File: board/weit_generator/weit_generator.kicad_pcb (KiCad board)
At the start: 2 copper layers, 58 parts, among them J1 POWER, J2 PROG, J3 OUTPUT, Q1 BC547, U1 MCP6004, U2 AVR32DA28x-xSO, U3 LM4041L, U4 LMV321, X1 SG-5032CAN

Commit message: .
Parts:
- moved C1 83.8 mm to (131.2, 80.8), turned to 180 degrees
- moved J2 76.5 mm to (123.2, 91.8), turned to 180 degrees
- moved J1 41.5 mm to (131.3, 86.8), turned to -90 degrees
- moved C7 40.4 mm to (138.1, 86.1)
- moved C6 39.7 mm to (138.1, 79.5)
- moved J3 39.5 mm to (148.4, 93.1)
- moved C4 38.9 mm to (127.3, 92.9), turned to 0 degrees
- moved U4 25.2 mm to (142.8, 93.2), turned to 180 degrees
- moved Q1 19.4 mm to (116.4, 130.4), turned to 0 degrees
- moved R2 18.0 mm to (126.6, 104.7), turned to -90 degrees
- moved R29 17.7 mm to (112.9, 125.0)
- moved RV1 17.1 mm to (123.4, 117.6), turned to 90 degrees
- moved TP3 14.7 mm to (149.1, 127.0)
- moved C2 14.1 mm to (117.8, 122.7), turned to 90 degrees
- moved R27 13.3 mm to (122.1, 125.7), turned to 0 degrees
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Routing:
- net +3V0: track 33.2 -> 134.4 mm
- net GND: track 11.6 -> 27.8 mm
- net Net-(U1C--): track 38.2 -> 24.2 mm
- net /Autogain/OUT: track 4.72 -> 17.5 mm
- net Net-(U1A--): track 9.35 -> 19.3 mm
- net /R-2R DAC/OUT: track 3.57 -> 12.3 mm
- net Net-(J2-Pin_2): track 5.18 -> 12.8 mm
- net Net-(U1C-+): track 13.5 -> 20.8 mm
- net Net-(C13-Pad1): track 26.1 -> 19.3 mm
- net Net-(C11-Pad2): track 21.5 -> 15.5 mm
- net Net-(U1D-+): track 12.7 -> 16.9 mm
- net Net-(J2-Pin_3): track 7.83 -> 11.3 mm
- net Net-(D2-K): track 3.44 -> 6.70 mm
- net Net-(U4--): track 18.0 -> 15.2 mm
- net Net-(U1A-+): track 26.3 -> 23.8 mm
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- added copper zone on F.Cu, net GND
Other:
- board outline added: 59.5 x 60.2 mm

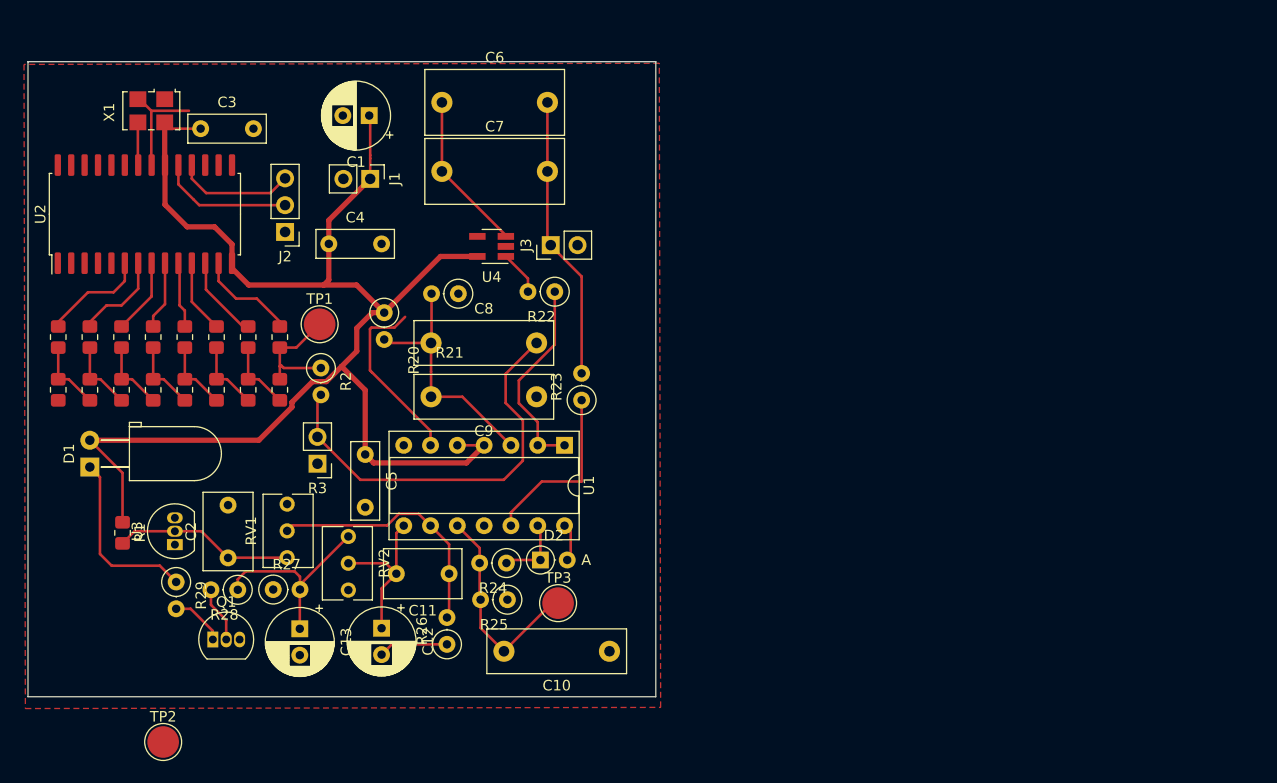
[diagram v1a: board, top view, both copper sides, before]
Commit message: finished board, added test desription and tuning to docs
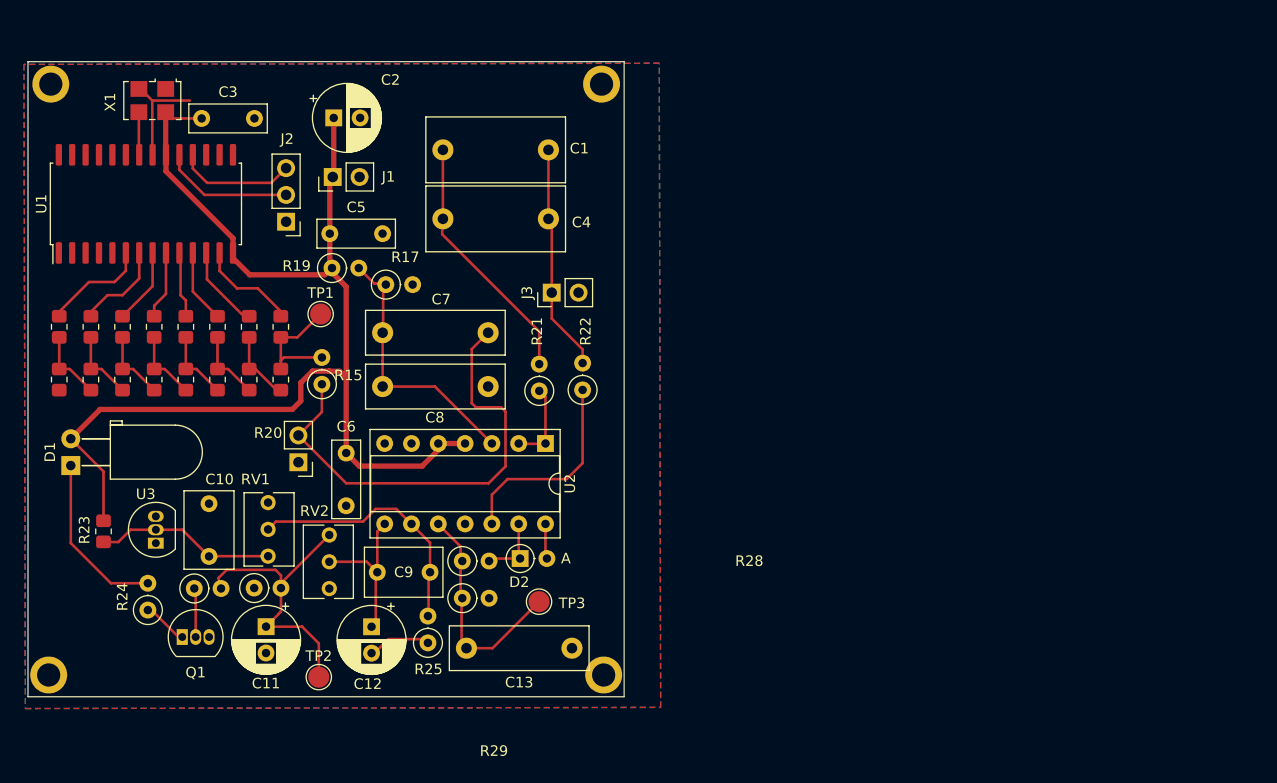
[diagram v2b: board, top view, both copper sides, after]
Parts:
- removed U4: LMV321, Package_TO_SOT_SMD:SOT-23-5_HandSoldering
- added REF**: MountingHole_2.2mm_M2_ISO7380_Pad, MountingHole:MountingHole_2.2mm_M2_ISO7380_Pad, F.Cu at (100.8, 133.8)
- added REF**: MountingHole_2.2mm_M2_ISO7380_Pad, MountingHole:MountingHole_2.2mm_M2_ISO7380_Pad, F.Cu at (101.0, 77.8)
- added REF**: MountingHole_2.2mm_M2_ISO7380_Pad, MountingHole:MountingHole_2.2mm_M2_ISO7380_Pad, F.Cu at (153.2, 77.8)
- added REF**: MountingHole_2.2mm_M2_ISO7380_Pad, MountingHole:MountingHole_2.2mm_M2_ISO7380_Pad, F.Cu at (153.4, 133.8)
- TP1, TP2, TP3: footprint TestPoint:TestPoint_Pad_D3.0mm -> TestPoint:TestPoint_Pad_D2.0mm
- moved TP2 16.0 mm to (126.4, 134.0)
- moved R21 9.52 mm to (147.3, 106.9), turned to 90 degrees
- moved R17 6.92 mm to (132.8, 96.8), turned to 0 degrees
- moved R19 6.51 mm to (127.7, 95.2), turned to 0 degrees
- moved C8 4.69 mm to (142.4, 106.5)
- moved C7 4.69 mm to (132.4, 101.4)
- moved C1 4.50 mm to (138.2, 84.0)
- moved C4 4.50 mm to (138.2, 90.6)
- moved J3 4.50 mm to (148.5, 97.6)
- moved R29 4.28 mm to (140.0, 126.5), turned to 0 degrees
- moved R28 4.19 mm to (140.0, 123.0), turned to 0 degrees
- moved R26 4.12 mm to (114.6, 125.6), turned to 0 degrees
- moved R24 3.78 mm to (110.2, 127.6), turned to 90 degrees
- moved C13 3.57 mm to (150.4, 131.3)
- moved J1 3.55 mm to (127.7, 86.6), turned to 90 degrees
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- renumbered C6 to C1, C2 to C10, C13 to C11, C10 to C13, C1 to C2, C7 to C4, C4 to C5, C5 to C6, C8 to C7, C9 to C8, C11 to C9, R10 to R1, R7 to R10, R4 to R11, R13 to R12, R14 to R13, R12 to R14, R2 to R15, R6 to R16, R21 to R17, R5 to R18, R20 to R19, R17 to R2, R3 to R20, R22 to R21, R23 to R22, R1 to R23, R29 to R24, R26 to R25, R28 to R26, R24 to R28, R25 to R29, R11 to R3, R19 to R4, R16 to R5, R9 to R6, R15 to R7, R18 to R8, R8 to R9, U2 to U1, U1 to U2
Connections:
- C1 pad 1: Net-(U4--) -> /Output Filter/OUT
- C4 pad 1: Net-(U4--) -> /Output Filter/OUT
- R15 pad 1: /R-2R DAC/OUT -> /Output Filter/IN
- R15 pad 2: /Output Filter/IN -> /R-2R DAC/OUT
- R17 pad 1: GND -> Net-(U1A-+)
- R17 pad 2: Net-(U1A-+) -> GND
- R24 pad 1: /Autogain/OUT -> Net-(Q1-C)
- R24 pad 2: Net-(Q1-C) -> /Autogain/OUT
- R26 pad 1: Net-(C13-Pad1) -> Net-(Q1-B)
- R26 pad 2: Net-(Q1-B) -> Net-(C13-Pad1)
- R28 pad 1: Net-(D2-K) -> Net-(U1C-+)
- R28 pad 2: Net-(U1C-+) -> Net-(D2-K)
- R29 pad 1: GND -> Net-(U1C-+)
- R29 pad 2: Net-(U1C-+) -> GND
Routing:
- net /Output Filter/OUT: track 4.21 -> 24.1 mm
- net +3V0: track 134.4 -> 114.9 mm
- net GND: track 27.8 -> 10.5 mm
- net Net-(U4--): track 15.2 -> 0.00 mm
- net Net-(U1A--): track 19.3 -> 7.77 mm
- net Net-(C13-Pad1): track 19.3 -> 28.2 mm
- net /Autogain/IN: track 27.0 -> 21.6 mm
- net /Output Filter/IN: track 39.1 -> 44.0 mm
- net Net-(U1D-+): track 16.9 -> 19.5 mm
- net Net-(U1A-+): track 23.8 -> 25.3 mm
- net /Autogain/OUT: track 17.5 -> 16.2 mm
- net Net-(U1C-+): track 20.8 -> 21.6 mm
- net Net-(Q1-C): track 5.15 -> 4.46 mm
- net /R-2R DAC/OUT: track 12.3 -> 11.7 mm
- net Net-(C12-Pad2): track 6.60 -> 6.04 mm
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- added copper zone on B.Cu, net GND
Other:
- board size 59.5 x 60.2 mm -> 56.5 x 60.2 mm

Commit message: .
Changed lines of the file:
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@@
     (property "ki_keywords" "R res resistor")
     (attr through_hole)
-    (fp_text reference "R15" (at 0.845 2.505) (layer "F.SilkS")
+    (fp_text reference "R15" (at 1.045 2.705 90) (layer "F.SilkS")
         (effects (font (size 1 1) (thickness 0.15)))
     )

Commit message: .
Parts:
- removed REF** (x4): MountingHole_2.2mm_M2_ISO7380_Pad, MountingHole:MountingHole_2.2mm_M2_ISO7380_Pad
- C7: value 10n -> 100n; footprint Capacitor_THT:C_Rect_L13.0mm_W4.0mm_P10.00mm_FKS3_FKP3_MKS4 -> Capacitor_THT:C_Rect_L13.0mm_W6.0mm_P10.00mm_FKS3_FKP3_MKS4
- moved C7 9.97 mm to (142.4, 100.8), turned to 180 degrees
- moved R17 1.49 mm to (133.3, 95.4)
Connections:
- C7 pad 1: Net-(U1A-+) -> /Output Filter/IN
- C7 pad 2: /Output Filter/IN -> Net-(U2A-+)
- C8 pad 2: Net-(U1A-+) -> Net-(U2A-+)
- R17 pad 1: Net-(U1A-+) -> Net-(U2A-+)
- R19 pad 2: Net-(U1A-+) -> Net-(U2A-+)
- U2 pad 3: Net-(U1A-+) -> Net-(U2A-+)
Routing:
- net Net-(U2A-+): track 0.00 -> 27.2 mm
- net Net-(U1A-+): track 25.3 -> 0.00 mm

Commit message: WIELKA POLONIAAAAA
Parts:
- added ?: , , F.Cu at (101.2, 78.4)
- added ?: , , F.Cu at (153.2, 78.2)
- added ?: , , F.Cu at (153.2, 133.8)
- added REF**: MountingHole_2.2mm_M2_DIN965_Pad, MountingHole:MountingHole_2.2mm_M2_DIN965_Pad, F.Cu at (101.0, 133.6)
- J1: value POWER -> Zasilanie
- J3: value OUTPUT -> Wyjście
- moved C12 1.20 mm to (130.2, 129.2)
- moved R25 1.15 mm to (135.6, 130.6)
- moved C13 1.10 mm to (149.4, 130.8)
- moved TP2 0.60 mm to (125.8, 134.0)
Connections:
- net /Autogain/IN renamed /Kontrola Amplitiudy/IN
- net /Autogain/OUT renamed /Kontrola Amplitiudy/OUT
- net /Output Filter/IN renamed /Filtr Wyjściowy/IN
- net /Output Filter/OUT renamed /Filtr Wyjściowy/OUT
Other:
- board size 56.5 x 60.2 mm -> 56.3 x 59.7 mm

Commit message: potężny polski assembler
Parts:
- moved REF** 0.20 mm to (101.2, 133.6)
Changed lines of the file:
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@@
       (sketchpadsonfab false)
       (subtractmaskfromsilk false)
-      (outputformat 1)
+      (outputformat 4)
       (mirror false)
       (drillshape 0)
       (scaleselection 1)
-      (outputdirectory "grb")
+      (outputdirectory "../../../../")
     )
   )
@@
   )
   (footprint "MountingHole:MountingHole_2.2mm_M2_DIN965_Pad" (layer "F.Cu")
-    (at 101 133.6)
+    (at 101.2 133.6)
     (descr "Mounting Hole 2.2mm, M2, DIN965")
     (tags "mounting hole 2.2mm m2 din965")
@@
     (polygon
       (pts
-        (xy 155.595542 136.230795)
-        (xy 155.4 75)
-        (xy 98.255542 74.560795)
-        (xy 98.185542 137.210795)
+        (xy 155.4 136)
+        (xy 155.2 76.2)
+        (xy 99 76)
+        (xy 99 136)
       )
     )

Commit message: Final revision - submitting
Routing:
- net Net-(U2D-+): track 19.5 -> 18.9 mm
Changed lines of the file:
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@@
     (property "ki_keywords" "R res resistor")
     (attr through_hole)
-    (fp_text reference "R28" (at 27.2 0) (layer "F.SilkS")
+    (fp_text reference "R28" (at 27.2 0) (layer "F.SilkS") hide
         (effects (font (size 1 1) (thickness 0.15)))
     )
@@
     (property "ki_keywords" "R res resistor")
     (attr through_hole)
-    (fp_text reference "R29" (at 3 14.48) (layer "F.SilkS")
+    (fp_text reference "R29" (at 3 14.48) (layer "F.SilkS") hide
         (effects (font (size 1 1) (thickness 0.15)))
     )
@@
   (segment (start 115.8 93.87) (end 115.73 93.8) (width 0.25) (layer "F.Cu") (net 10))
   (segment (start 130.36 95.4) (end 130.19 95.23) (width 0.25) (layer "F.Cu") (net 11))
-  (segment (start 142.805 111.86) (end 137.405 106.46) (width 0.25) (layer "F.Cu") (net 11))
+  (segment (start 137.86 106.46) (end 132.45 106.46) (width 0.25) (layer "F.Cu") (net 11))
   (segment (start 133.26 95.4) (end 130.36 95.4) (width 0.25) (layer "F.Cu") (net 11))
-  (segment (start 137.405 106.46) (end 132.45 106.46) (width 0.25) (layer "F.Cu") (net 11))
   (segment (start 133.26 99.94) (end 132.4 100.8) (width 0.25) (layer "F.Cu") (net 11))
   (segment (start 132.45 100.85) (end 132.4 100.8) (width 0.25) (layer "F.Cu") (net 11))
+  (segment (start 142.805 111.86) (end 142.805 111.405) (width 0.25) (layer "F.Cu") (net 11))
   (segment (start 133.26 95.4) (end 133.26 99.94) (width 0.25) (layer "F.Cu") (net 11))
   (segment (start 132.45 106.46) (end 132.45 100.85) (width 0.25) (layer "F.Cu") (net 11))
+  (segment (start 142.805 111.405) (end 137.86 106.46) (width 0.25) (layer "F.Cu") (net 11))
   (segment (start 116.8 99.8) (end 114.46 97.46) (width 0.25) (layer "F.Cu") (net 12))
   (segment (start 114.46 97.46) (end 114.46 93.8) (width 0.25) (layer "F.Cu") (net 12))
@@
   (segment (start 147.885 111.86) (end 147.885 107.465) (width 0.25) (layer "F.Cu") (net 29))
   (segment (start 147.885 107.465) (end 147.295 106.875) (width 0.25) (layer "F.Cu") (net 29))
-  (segment (start 149.895 115.23) (end 144.295 115.23) (width 0.25) (layer "F.Cu") (net 30))
   (segment (start 151.405 113.72) (end 149.895 115.23) (width 0.25) (layer "F.Cu") (net 30))
+  (segment (start 149.895 115.23) (end 145.37 115.23) (width 0.25) (layer "F.Cu") (net 30))
+  (segment (start 142.805 117.795) (end 142.805 119.48) (width 0.25) (layer "F.Cu") (net 30))
+  (segment (start 145.37 115.23) (end 142.805 117.795) (width 0.25) (layer "F.Cu") (net 30))
   (segment (start 151.405 106.78) (end 151.405 113.72) (width 0.25) (layer "F.Cu") (net 30))
-  (segment (start 142.805 116.72) (end 142.805 119.48) (width 0.25) (layer "F.Cu") (net 30))
-  (segment (start 144.295 115.23) (end 142.805 116.72) (width 0.25) (layer "F.Cu") (net 30))
   (segment (start 109.35 80.455) (end 109.35 84.47) (width 0.25) (layer "F.Cu") (net 38))
   (segment (start 109.35 84.47) (end 109.38 84.5) (width 0.25) (layer "F.Cu") (net 38))
@@
   (segment (start 151.405 104.24) (end 151.405 102.94) (width 0.25) (layer "F.Cu") (net 53))
   (segment (start 148.48 90.885) (end 148.165 90.57) (width 0.25) (layer "F.Cu") (net 53))
+  (segment (start 142.495 115.63) (end 144.095 114.03) (width 0.25) (layer "F.Cu") (net 54))
+  (segment (start 144.095 114.03) (end 144.095 109.495) (width 0.25) (layer "F.Cu") (net 54))
   (segment (start 124.47 111.095) (end 129.005 115.63) (width 0.25) (layer "F.Cu") (net 54))
-  (segment (start 144.095 114.03) (end 144.095 108.83) (width 0.25) (layer "F.Cu") (net 54))
   (segment (start 126.695 108.87) (end 124.47 111.095) (width 0.25) (layer "F.Cu") (net 54))
-  (segment (start 129.005 115.63) (end 142.495 115.63) (width 0.25) (layer "F.Cu") (net 54))
   (segment (start 141.295 108.43) (end 140.895 108.03) (width 0.25) (layer "F.Cu") (net 54))
   (segment (start 126.695 106.275) (end 126.695 108.87) (width 0.25) (layer "F.Cu") (net 54))
-  (segment (start 140.895 102.915) (end 142.45 101.36) (width 0.25) (layer "F.Cu") (net 54))
-  (segment (start 142.495 115.63) (end 144.095 114.03) (width 0.25) (layer "F.Cu") (net 54))
-  (segment (start 140.895 108.03) (end 140.895 102.915) (width 0.25) (layer "F.Cu") (net 54))
-  (segment (start 143.695 108.43) (end 141.295 108.43) (width 0.25) (layer "F.Cu") (net 54))
-  (segment (start 144.095 108.83) (end 143.695 108.43) (width 0.25) (layer "F.Cu") (net 54))
+  (segment (start 129.005 115.63) (end 142.495 115.63) (width 0.25) (layer "F.Cu") (net 54))
+  (segment (start 143.03 108.43) (end 141.295 108.43) (width 0.25) (layer "F.Cu") (net 54))
+  (segment (start 144.095 109.495) (end 143.03 108.43) (width 0.25) (layer "F.Cu") (net 54))
+  (segment (start 140.895 108.03) (end 140.895 101.905) (width 0.25) (layer "F.Cu") (net 54))
+  (segment (start 140.895 101.905) (end 141.44 101.36) (width 0.25) (layer "F.Cu") (net 54))
+  (segment (start 141.44 101.36) (end 142.45 101.36) (width 0.25) (layer "F.Cu") (net 54))
   (segment (start 110.2 125.105) (end 106.705 125.105) (width 0.25) (layer "F.Cu") (net 55))
   (segment (start 102.895 121.295) (end 102.895 113.95) (width 0.25) (layer "F.Cu") (net 55))
